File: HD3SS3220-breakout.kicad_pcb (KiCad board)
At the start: 4 copper layers, 30.6 x 52 mm, 31 parts, among them J1 USB_C_Receptacle, J2 U-A-39SS-Y-1, J3 A2541WV-2x4P, SW1 SW_DIP_x04, U1 HD3SS3220RNHR, U2 TPD2EUSB30, U3 TPD4EUSB30, U4 HT7533-1_C14289

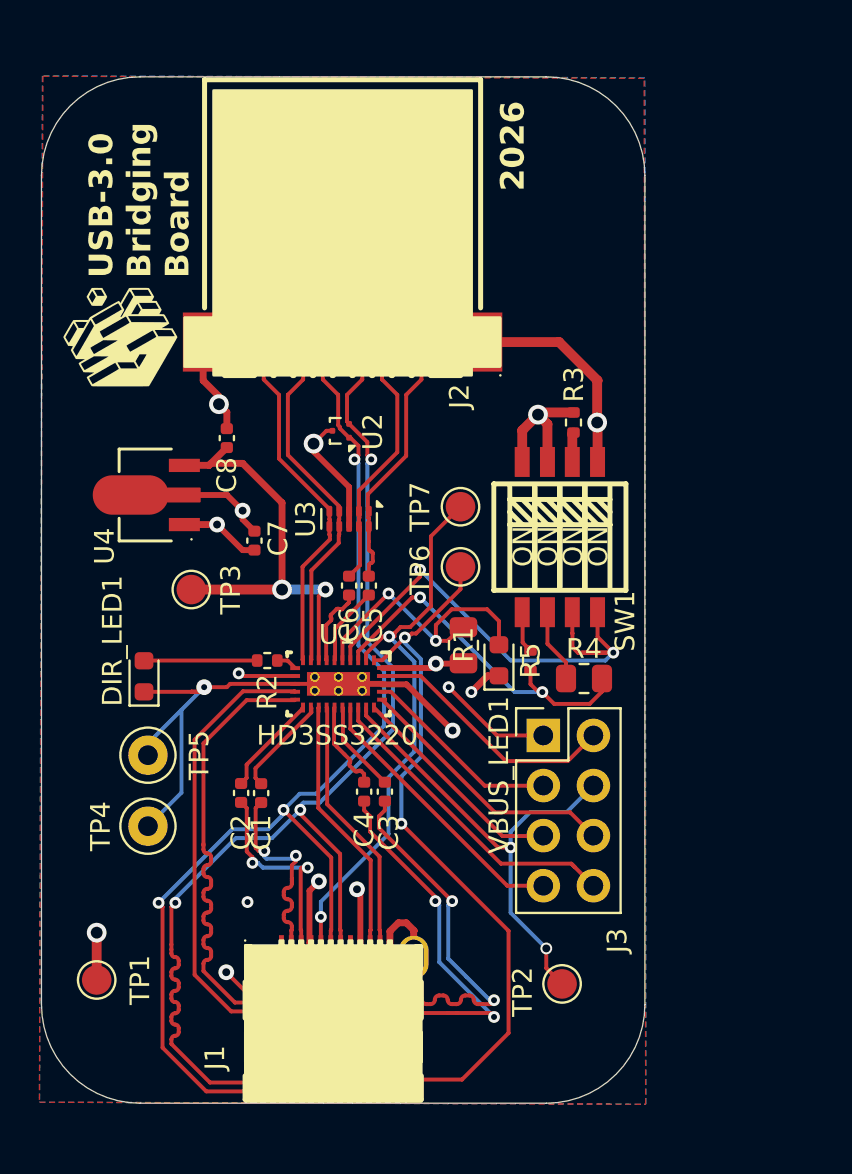
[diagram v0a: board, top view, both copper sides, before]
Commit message: Add Screenshots for README
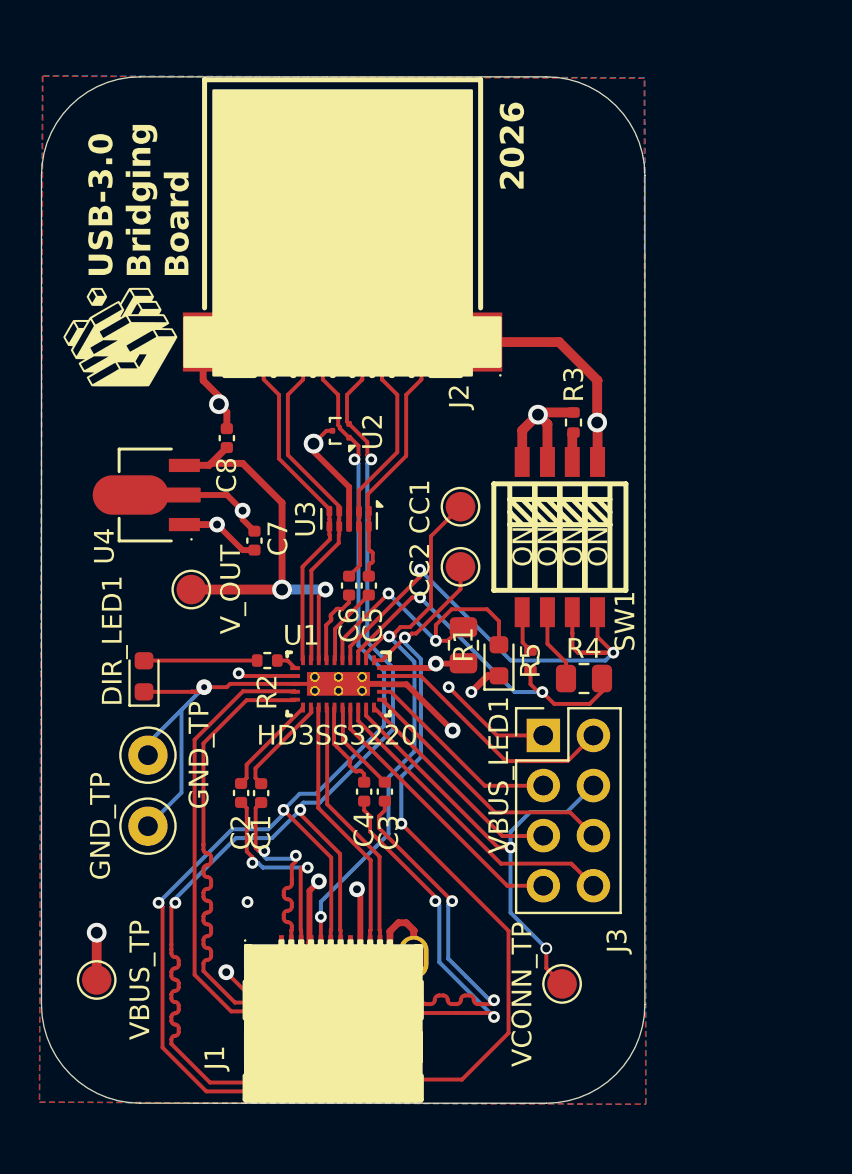
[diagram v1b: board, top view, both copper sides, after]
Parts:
- renumbered TP7 to CC1, TP6 to CC2, TP4 to GND_TP, TP5 to GND_TP, TP1 to VBUS_TP, TP2 to VCONN_TP, TP3 to V_OUT
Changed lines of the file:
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@@
 		(descr "SMD pad as test Point, diameter 1.5mm")
 		(tags "test point SMD pad")
-		(property "Reference" "TP6"
+		(property "Reference" "CC2"
 			(at -2.05 0.15 90)
 			(layer "F.SilkS")
@@
 		(descr "Keystone THM Miniature Test Point 5000-5004, http://www.keyelco.com/product-pdf.cfm?p=1309")
 		(tags "Through Hole Mount Test Points")
-		(property "Reference" "TP4"
+		(property "Reference" "GND_TP"
 			(at -2.4 0 270)
 			(layer "F.SilkS")
@@
 		(descr "SMD pad as test Point, diameter 1.5mm")
 		(tags "test point SMD pad")
-		(property "Reference" "TP7"
+		(property "Reference" "CC1"
 			(at -2.05 0 90)
 			(layer "F.SilkS")
@@
 		(descr "SMD pad as test Point, diameter 1.5mm")
 		(tags "test point SMD pad")
-		(property "Reference" "TP2"
-			(at -2 0.4 90)
+		(property "Reference" "VCONN_TP"
+			(at -2.02 0.53 90)
 			(layer "F.SilkS")
 			(effects
@@
 		(descr "SMD pad as test Point, diameter 1.5mm")
 		(tags "test point SMD pad")
-		(property "Reference" "TP3"
+		(property "Reference" "V_OUT"
 			(at 2 0 90)
 			(layer "F.SilkS")
@@
 		(descr "Keystone THM Miniature Test Point 5000-5004, http://www.keyelco.com/product-pdf.cfm?p=1309")
 		(tags "Through Hole Mount Test Points")
-		(property "Reference" "TP5"
+		(property "Reference" "GND_TP"
 			(at 2.6 0 90)
 			(layer "F.SilkS")
@@
 		(descr "SMD pad as test Point, diameter 1.5mm")
 		(tags "test point SMD pad")
-		(property "Reference" "TP1"
+		(property "Reference" "VBUS_TP"
 			(at 2.2 0 90)
 			(layer "F.SilkS")
@@
 		(tags "HD3SS3220IRNHR ")
 		(property "Reference" "U1"
-			(at -2.5 0.0624 0)
+			(at -2.454399 1.8824 0)
 			(unlocked yes)
 			(layer "F.SilkS")

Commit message: Protruding USB connectors for easier CAD design
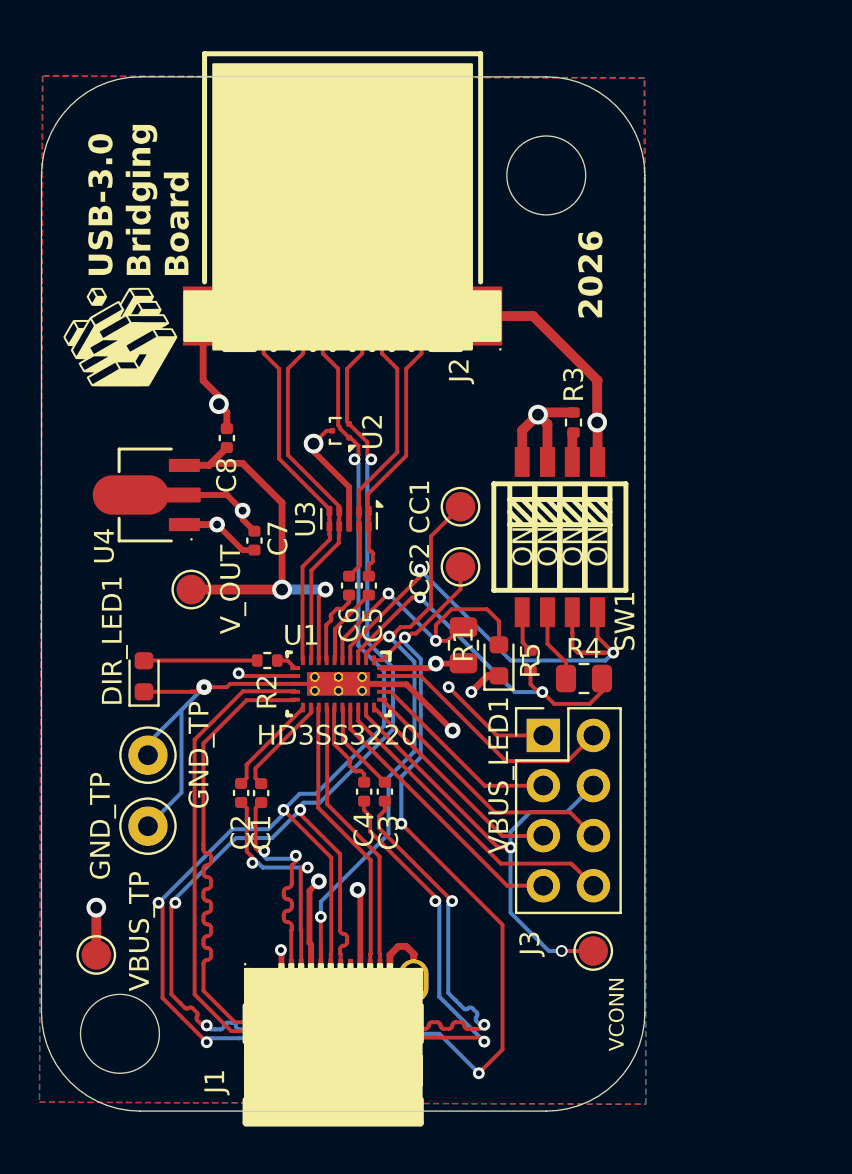
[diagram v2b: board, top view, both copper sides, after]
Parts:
- moved VCONN 2.30 mm to (114.4, 79.6)
- moved J2 1.32 mm to (101.7, 47.8)
- moved VBUS_TP 1.27 mm to (89.2, 79.8)
- moved J1 1.20 mm to (101.2, 83.1)
- renumbered VCONN_TP to VCONN
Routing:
- net VBUS: track 38.4 -> 40.7 mm
- net /Type-C Interface & High-Speed Mux/CC1: track 28.5 -> 30.6 mm
- net /Type-A Interface/D+: track 64.5 -> 62.7 mm, vias 3 -> 5
- net /Type-A Interface/D-: track 64.2 -> 62.7 mm, vias 3 -> 5
- net /Type-A Interface/SSRX-: track 17.5 -> 18.8 mm
- net /Type-A Interface/SSTX-: track 12.6 -> 13.9 mm
- net /Type-A Interface/SSTX+: track 12.6 -> 13.9 mm
- net /Type-A Interface/SSRX+: track 17.5 -> 18.8 mm
- net /Type-C Interface & High-Speed Mux/TX1-: track 10.4 -> 11.6 mm
- net /Type-C Interface & High-Speed Mux/TX1+: track 10.4 -> 11.6 mm
- net /Type-C Interface & High-Speed Mux/RX2-: track 13.1 -> 14.3 mm
- net /Type-C Interface & High-Speed Mux/RX2+: track 13.1 -> 14.3 mm
- net /Type-C Interface & High-Speed Mux/CC2: track 43.2 -> 42.2 mm, vias 2 -> 4
- net /Type-C Interface & High-Speed Mux/RX1-: track 25.8 -> 26.8 mm
- net /Type-C Interface & High-Speed Mux/RX1+: track 25.6 -> 26.6 mm
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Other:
- board size 30.6 x 52 mm -> 30.6 x 52.4 mm

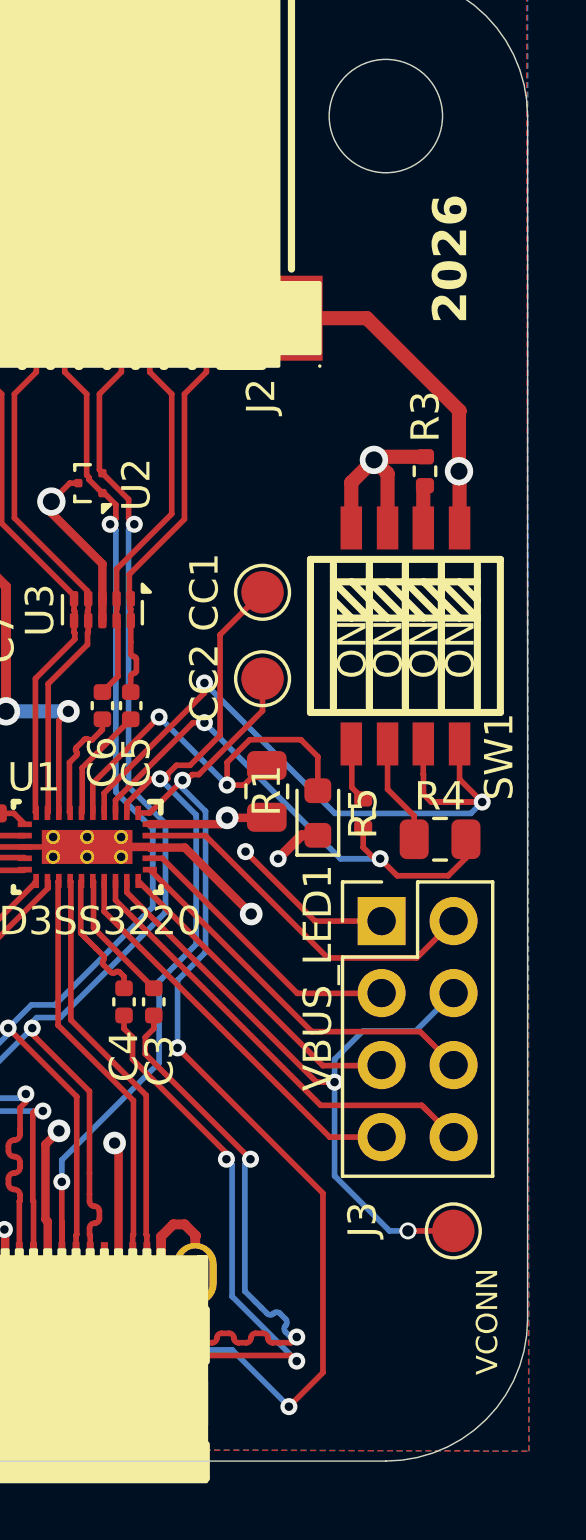
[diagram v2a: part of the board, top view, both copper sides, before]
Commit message: Holes drilled for easier case CAD design
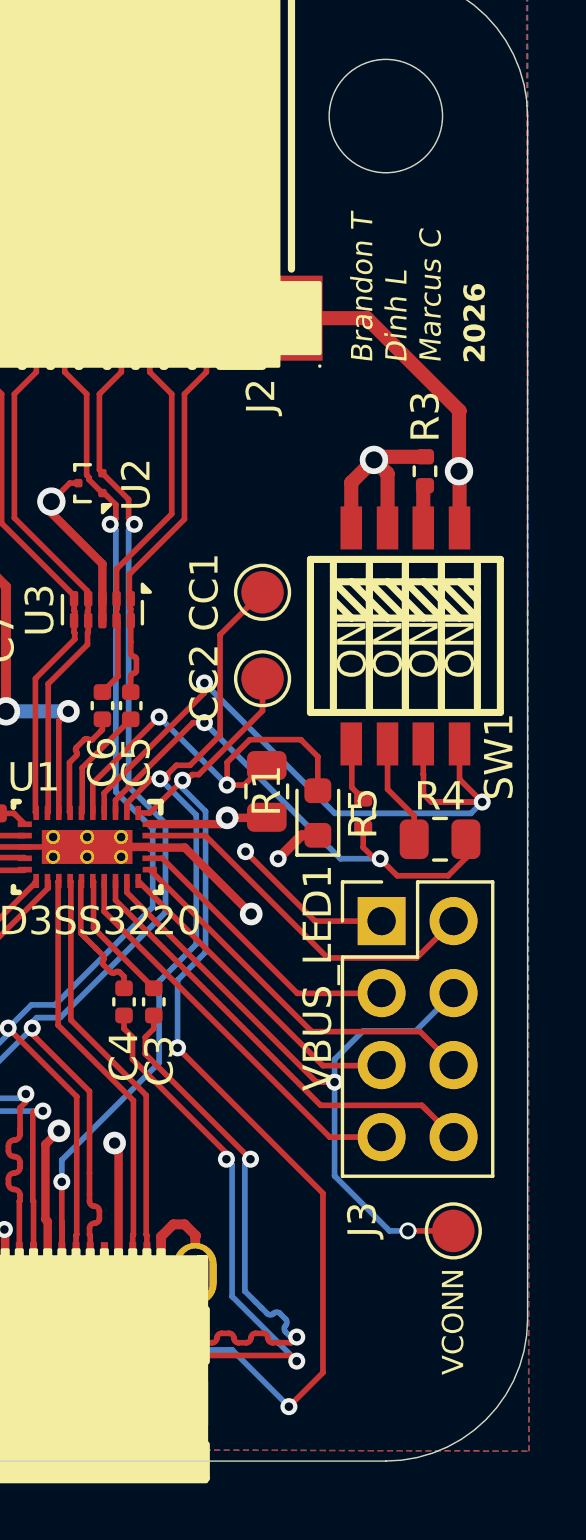
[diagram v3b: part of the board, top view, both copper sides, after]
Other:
- board text added: "Brandon T Dinh L Marcus C"
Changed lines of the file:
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@@
 		(tags "test point SMD pad")
 		(property "Reference" "VCONN"
-			(at 1.2 3.2 90)
+			(at 0 3.2 90)
 			(layer "F.SilkS")
 			(effects
@@
 		(layer "Edge.Cuts")
 	)
-	(gr_text "USB-3.0\nBridging\nBoard"
-		(at 94.02 45.47 90)
+	(gr_text "2026"
+		(at 115.6 49 90)
 		(layer "F.SilkS")
 		(effects
 			(font
-				(size 1.2 1.2)
+				(size 0.75 0.75)
 				(bold yes)
 			)
@@
 		)
 	)
-	(gr_text "2026"
-		(at 115 47.6 90)
+	(gr_text "Brandon T\nDinh L\nMarcus C"
+		(at 112.4 49 90)
+		(layer "F.SilkS")
+		(effects
+			(font
+				(size 0.75 0.75)
+				(thickness 0.09375)
+				(italic yes)
+			)
+			(justify left)
+		)
+	)
+	(gr_text "USB-3.0\nBridging\nBoard"
+		(at 94.02 45.47 90)
 		(layer "F.SilkS")
 		(effects
@@
 		(layer "Cmts.User")
 		(pts
-			(xy 112.02 87.32) (xy 112.02 35.270001)
+			(xy 112.02 87.72) (xy 112.02 35.27)
 		)
 		(height 13.849174)
@@
 			(keep_text_aligned yes)
 		)
-		(gr_text "52.05"
-			(at 124.069174 61.295 90)
+		(gr_text "52.45"
+			(at 124.069174 61.495 90)
 			(layer "Cmts.User")
 			(effects
@@
 		)
 		(min_thickness 0.25)
-		(fill
+		(fill yes
 			(thermal_gap 0.5)
 			(thermal_bridge_width 0.5)
@@
 		)
 		(min_thickness 0.25)
-		(fill
+		(fill yes
 			(thermal_gap 0.5)
 			(thermal_bridge_width 0.5)
@@
 		)
 		(min_thickness 0.25)
-		(fill
+		(fill yes
 			(thermal_gap 0.5)
 			(thermal_bridge_width 0.5)
@@
 		)
 		(min_thickness 0.25)
-		(fill
+		(fill yes
 			(thermal_gap 0.5)
 			(thermal_bridge_width 0.5)
